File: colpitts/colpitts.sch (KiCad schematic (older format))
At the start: 24 parts

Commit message: Update diseño esquemático
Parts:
- added C? (x2): 100nF, symbol Device:C
- added Q?: 2N3904, Package_TO_SOT_THT:TO-92_Inline, symbol Transistor_BJT:2N3904
- added R? (x4): R, symbol Device:R
- added RV?: R_POT, symbol Device:R_POT
- added U?: LM741, symbol Amplifier_Operational:LM741
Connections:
- net GND: now also C?.1, R?.1, R?.1
- net at JP?.2 (B): now also Q?.2 (B), R?.2
- new net: C?.2, Q?.1 (E), R?.1, R?.2
- new net: C?.2, R?.2, U?.2 (-)
- new net: C?.1, R?.2
- new net +12V: Q?.3 (C)
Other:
- moved on the sheet: C?, J?, JP?, L?, Q?, R?

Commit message: Update diseño esquemático (previa anotación componentes)
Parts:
- removed C?: 100nF, symbol Device:C
- removed R?: R, symbol Device:R
- added C?: 100nF, symbol Device:C
- added C?: 10nF, symbol Device:C
- added J?: BORNERA, symbol Connector_Generic:Conn_01x04
- added R? (x3): 1K, symbol Device:R
- C?: value 100nF -> 100pF
- C?: value 100nF -> 15pF
- C?: value 100nF -> 68pF
- C?: value CTRIM -> TRIM VERDE (5.2pF-30pF)
- C?: value 100nF -> 10pF
- C?: value 100nF -> 33pF
- J?: value Conn_Coaxial -> BNC
- L?: value L -> 40n
- R? (x3): value R -> 10K
- R? (x2): value R -> 330
- R?: value R -> 3.9K
- R?: value R -> 5.6K
- R?: value R -> 1K
- RV?: value R_POT -> 10K
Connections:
- net +12V is gone; now on net +15V: Q?.3 (C)
- net +15V: now also U?.7 (V+), C?.1, J?.4 (Pin_4), R?.2
- net -15V: now also U?.4 (V-), J?.1 (Pin_1)
- net GND: now also C?.1, C?.2, J?.2 (Pin_2), J?.3 (Pin_3), R?.1
- net Vcontrol: now also R?.1, U?.6
- net at Q?.1 (E), R?.2: now also C?.2, R?.1
- net at C?.2, U?.2 (-): now also R?.2
- net at U?.3 (+): now also RV?.2
- net at RV?.1: now also R?.1
- net at RV?.3: now also R?.2
- no-connect marks 0 -> 2
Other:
- moved on the sheet: C?, J?, JP?, L?, Q?, R?, RV?, U?

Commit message: Update diseño esquemático (anotación de componentes)
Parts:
- gave numbers to parts that had none: 37

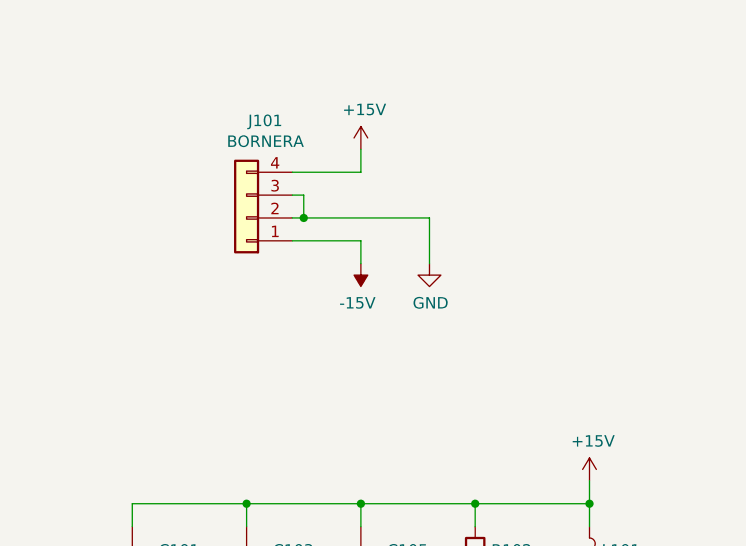
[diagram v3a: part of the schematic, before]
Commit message: ERC - Corrección de errores
1. POWER FLAGS de alimentación.
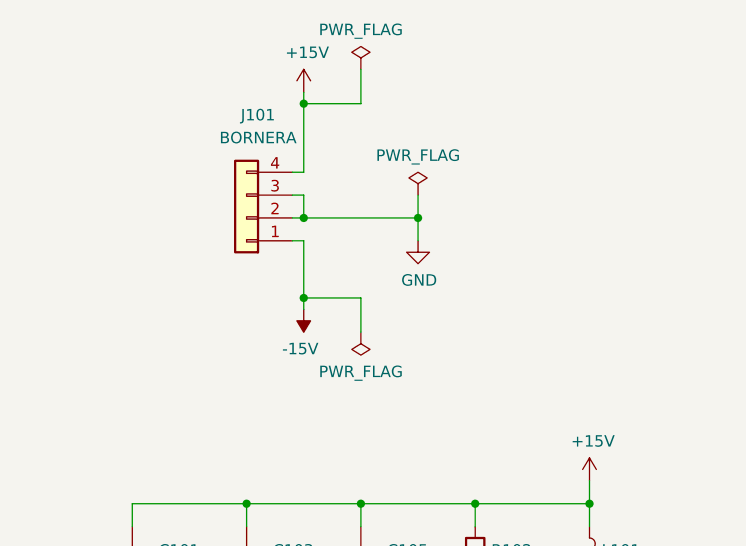
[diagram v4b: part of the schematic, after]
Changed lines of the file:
@@
 Wire Wire Line
 	4500 4250 4500 4300
-$Comp
-L power:GND #PWR0108
-U 1 1 5CF23D89
-P 5000 4800
-F 0 "#PWR0108" H 5000 4550 50  0001 C CNN
-F 1 "GND" H 5005 4627 50  0000 C CNN
-F 2 "" H 5000 4800 50  0001 C CNN
-F 3 "" H 5000 4800 50  0001 C CNN
-	1    5000 4800
-	1    0    0    -1
-$EndComp
 Wire Wire Line
 	5000 4100 5000 4700
@@
 	4500 4700 5000 4700
 Connection ~ 5000 4700
-Wire Wire Line
-	5000 4700 5000 4800
 Wire Wire Line
 	5500 4600 5500 4700
@@
 Wire Wire Line
 	8900 3600 9400 3600
+Wire Wire Line
+	9600 2750 9600 2925
+Wire Wire Line
+	8900 3075 8900 3600
+Wire Wire Line
+	9450 2925 9600 2925
+Connection ~ 9600 2925
+Wire Wire Line
+	9600 2925 9600 3400
+Wire Wire Line
+	9600 2925 10100 2925
+Wire Wire Line
+	10100 2925 10100 3000
+$Comp
+L Device:C C113
+U 1 1 5CFC3836
+P 8000 4100
+F 0 "C113" H 7825 4050 50  0000 C CNN
+F 1 "10nF" H 7800 4150 50  0000 C CNN
+F 2 "" H 8038 3950 50  0001 C CNN
+F 3 "~" H 8000 4100 50  0001 C CNN
+	1    8000 4100
+	-1   0    0    1
+$EndComp
+Connection ~ 8900 3800
+Wire Wire Line
+	8900 3800 9400 3800
+Wire Wire Line
+	8900 4650 8900 4700
+Wire Wire Line
+	8900 4700 10100 4700
+Wire Wire Line
+	10100 3700 10100 4700
+$Comp
+L Connector_Generic:Conn_01x04 J101
+U 1 1 5CFCE8BF
+P 2500 1600
+F 0 "J101" H 2450 1150 50  0000 C CNN
+F 1 "BORNERA" H 2450 1250 50  0000 C CNN
+F 2 "" H 2500 1600 50  0001 C CNN
+F 3 "~" H 2500 1600 50  0001 C CNN
+	1    2500 1600
+	-1   0    0    1
+$EndComp
+$Comp
+L power:+15V #PWR0103
+U 1 1 5CFCFA1F
+P 2750 1050
+F 0 "#PWR0103" H 2750 900 50  0001 C CNN
+F 1 "+15V" H 2765 1223 50  0000 C CNN
+F 2 "" H 2750 1050 50  0001 C CNN
+F 3 "" H 2750 1050 50  0001 C CNN
+	1    2750 1050
+	1    0    0    -1
+$EndComp
+$Comp
+L power:-15V #PWR0104
+U 1 1 5CFCFE1A
+P 2750 2000
+F 0 "#PWR0104" H 2750 2100 50  0001 C CNN
+F 1 "-15V" H 2765 2173 50  0000 C CNN
+F 2 "" H 2750 2000 50  0001 C CNN
+F 3 "" H 2750 2000 50  0001 C CNN
+	1    2750 2000
+	-1   0    0    1
+$EndComp
+Wire Wire Line
+	2700 1600 2750 1600
+Wire Wire Line
+	2700 1500 2750 1500
+Wire Wire Line
+	2750 1500 2750 1600
+Wire Wire Line
+	5000 4700 5000 4800
+$Comp
+L power:GND #PWR0108
+U 1 1 5CF23D89
+P 5000 4800
+F 0 "#PWR0108" H 5000 4550 50  0001 C CNN
+F 1 "GND" H 5005 4627 50  0000 C CNN
+F 2 "" H 5000 4800 50  0001 C CNN
+F 3 "" H 5000 4800 50  0001 C CNN
+	1    5000 4800
+	1    0    0    -1
+$EndComp
 $Comp
 L power:GND #PWR0115
@@
 	1    0    0    -1
 $EndComp
-Wire Wire Line
-	9600 2750 9600 2925
-Wire Wire Line
-	8900 3075 8900 3600
-Wire Wire Line
-	9450 2925 9600 2925
-Connection ~ 9600 2925
-Wire Wire Line
-	9600 2925 9600 3400
-Wire Wire Line
-	9600 2925 10100 2925
-Wire Wire Line
-	10100 2925 10100 3000
-$Comp
-L Device:C C113
-U 1 1 5CFC3836
-P 8000 4100
-F 0 "C113" H 7825 4050 50  0000 C CNN
-F 1 "10nF" H 7800 4150 50  0000 C CNN
-F 2 "" H 8038 3950 50  0001 C CNN
-F 3 "~" H 8000 4100 50  0001 C CNN
-	1    8000 4100
-	-1   0    0    1
-$EndComp
-Connection ~ 8900 3800
-Wire Wire Line
-	8900 3800 9400 3800
-Wire Wire Line
-	8900 4650 8900 4700
-Wire Wire Line
-	8900 4700 10100 4700
-Wire Wire Line
-	10100 3700 10100 4700
-$Comp
-L Connector_Generic:Conn_01x04 J101
-U 1 1 5CFCE8BF
-P 2500 1600
-F 0 "J101" H 2418 1175 50  0000 C CNN
-F 1 "BORNERA" H 2418 1266 50  0000 C CNN
-F 2 "" H 2500 1600 50  0001 C CNN
-F 3 "~" H 2500 1600 50  0001 C CNN
-	1    2500 1600
-	-1   0    0    1
-$EndComp
-$Comp
-L power:+15V #PWR0103
-U 1 1 5CFCFA1F
-P 3000 1300
-F 0 "#PWR0103" H 3000 1150 50  0001 C CNN
-F 1 "+15V" H 3015 1473 50  0000 C CNN
-F 2 "" H 3000 1300 50  0001 C CNN
-F 3 "" H 3000 1300 50  0001 C CNN
-	1    3000 1300
-	1    0    0    -1
-$EndComp
-$Comp
-L power:-15V #PWR0104
-U 1 1 5CFCFE1A
-P 3000 1800
-F 0 "#PWR0104" H 3000 1900 50  0001 C CNN
-F 1 "-15V" H 3015 1973 50  0000 C CNN
-F 2 "" H 3000 1800 50  0001 C CNN
-F 3 "" H 3000 1800 50  0001 C CNN
-	1    3000 1800
-	-1   0    0    1
-$EndComp
 $Comp
 L power:GND #PWR0105
 U 1 1 5CFD0749
-P 3300 1800
-F 0 "#PWR0105" H 3300 1550 50  0001 C CNN
-F 1 "GND" H 3305 1627 50  0000 C CNN
-F 2 "" H 3300 1800 50  0001 C CNN
-F 3 "" H 3300 1800 50  0001 C CNN
-	1    3300 1800
-	1    0    0    -1
-$EndComp
-Wire Wire Line
-	2700 1400 3000 1400
-Wire Wire Line
-	3000 1400 3000 1300
-Wire Wire Line
-	2700 1600 2750 1600
-Wire Wire Line
-	3300 1600 3300 1800
-Wire Wire Line
-	2700 1500 2750 1500
-Wire Wire Line
-	2750 1500 2750 1600
+P 3250 1700
+F 0 "#PWR0105" H 3250 1450 50  0001 C CNN
+F 1 "GND" H 3255 1527 50  0000 C CNN
+F 2 "" H 3250 1700 50  0001 C CNN
+F 3 "" H 3250 1700 50  0001 C CNN
+	1    3250 1700
+	1    0    0    -1
+$EndComp
+$Comp
+L power:PWR_FLAG #FLG0101
+U 1 1 5D007D00
+P 3000 2100
+F 0 "#FLG0101" H 3000 2175 50  0001 C CNN
+F 1 "PWR_FLAG" H 3000 2273 50  0000 C CNN
+F 2 "" H 3000 2100 50  0001 C CNN
+F 3 "~" H 3000 2100 50  0001 C CNN
+	1    3000 2100
+	-1   0    0    1
+$EndComp
+$Comp
+L power:PWR_FLAG #FLG0102
+U 1 1 5D008F68
+P 3250 1500
+F 0 "#FLG0102" H 3250 1575 50  0001 C CNN
+F 1 "PWR_FLAG" H 3250 1673 50  0000 C CNN
+F 2 "" H 3250 1500 50  0001 C CNN
+F 3 "~" H 3250 1500 50  0001 C CNN
+	1    3250 1500
+	1    0    0    -1
+$EndComp
+Wire Wire Line
+	2700 1400 2750 1400
+Wire Wire Line
+	2750 1400 2750 1100
+$Comp
+L power:PWR_FLAG #FLG0103
+U 1 1 5D007236
+P 3000 950
+F 0 "#FLG0103" H 3000 1025 50  0001 C CNN
+F 1 "PWR_FLAG" H 3000 1123 50  0000 C CNN
+F 2 "" H 3000 950 50  0001 C CNN
+F 3 "~" H 3000 950 50  0001 C CNN
+	1    3000 950
+	1    0    0    -1
+$EndComp
+Wire Wire Line
+	3000 950  3000 1100
+Wire Wire Line
+	3000 1100 2750 1100
+Connection ~ 2750 1100
+Wire Wire Line
+	2750 1100 2750 1050
+Wire Wire Line
+	2700 1700 2750 1700
+Wire Wire Line
+	2750 1700 2750 1950
+Wire Wire Line
+	3000 2100 3000 1950
+Wire Wire Line
+	3000 1950 2750 1950
+Connection ~ 2750 1950
+Wire Wire Line
+	2750 1950 2750 2000
+Wire Wire Line
+	3250 1700 3250 1600
+Wire Wire Line
+	3250 1600 2750 1600
 Connection ~ 2750 1600
 Wire Wire Line
-	2750 1600 3300 1600
-Wire Wire Line
-	2700 1700 3000 1700
-Wire Wire Line
-	3000 1700 3000 1800
+	3250 1600 3250 1500
+Connection ~ 3250 1600
 $EndSCHEMATC

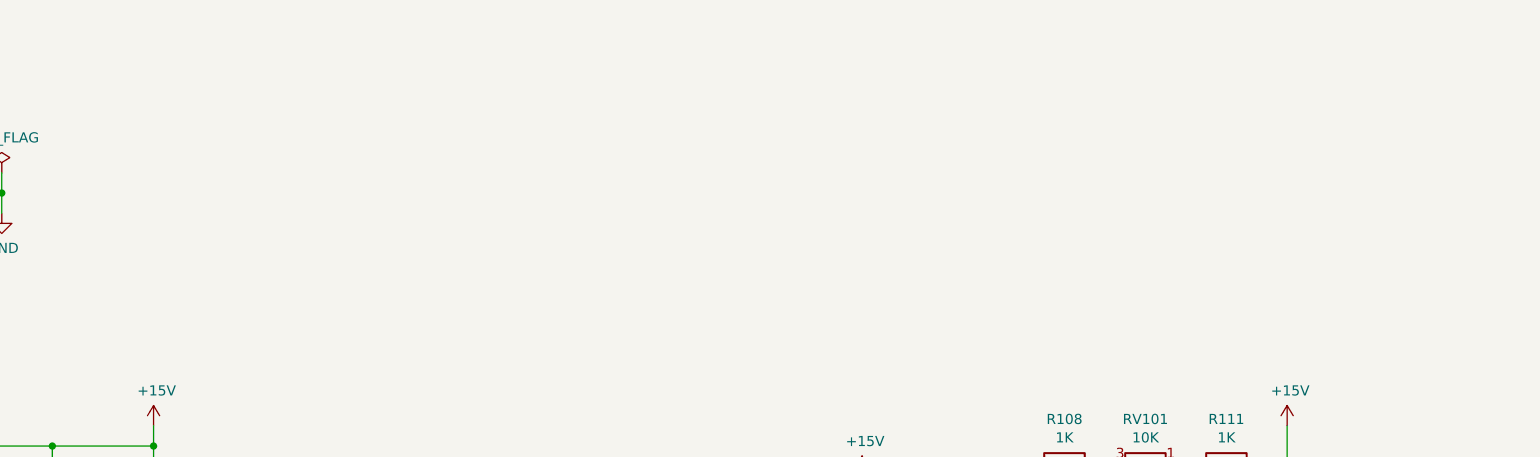
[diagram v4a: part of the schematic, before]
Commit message: Update diseño esquemático (previa asignación de huellas)
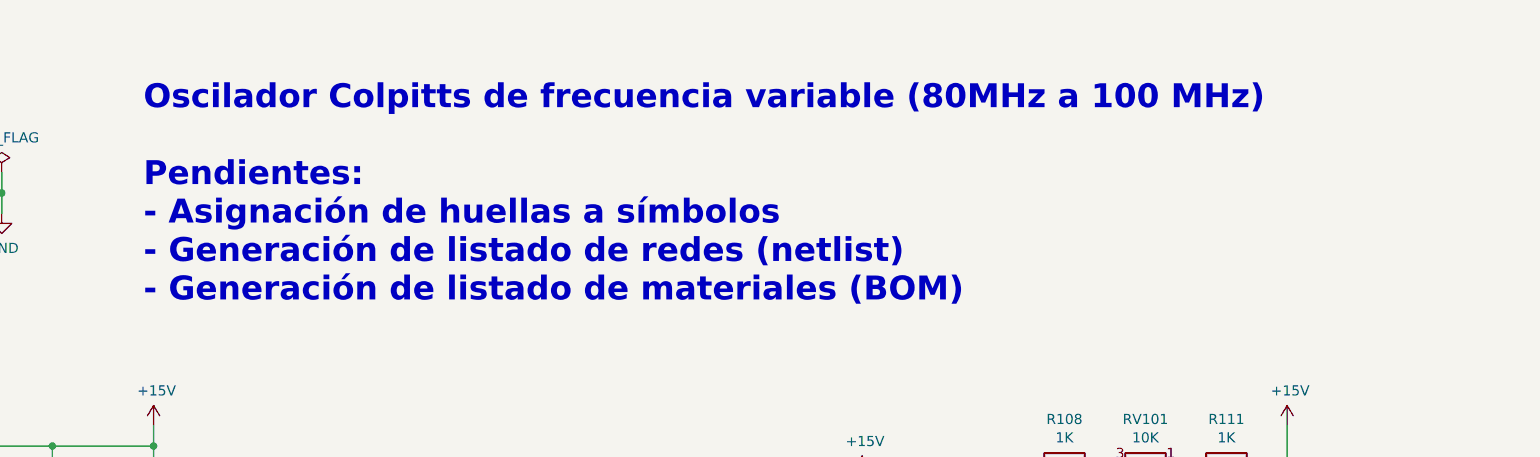
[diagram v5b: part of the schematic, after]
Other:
- note added: "Oscilador Colpitts de frecuencia variable (80MHz a 100 MHz)\n\nPendientes:\n- Asignación de huellas a símbolos\n- Generación de listado de redes (netlist)\n- Generación de listado de materiales (BOM)"
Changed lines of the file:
@@
 Text Label 6050 4250 2    79   Italic 16
 Vout
-Text Label 1500 4950 0    50   ~ 0
-Vcontrol
 $Comp
 L power:GND #PWR0109
@@
 	3250 1600 3250 1500
 Connection ~ 3250 1600
+Text Notes 3950 2150 0    118  ~ 24
+Oscilador Colpitts de frecuencia variable (80MHz a 100 MHz)\n\nPendientes:\n- Asignación de huellas a símbolos\n- Generación de listado de redes (netlist)\n- Generación de listado de materiales (BOM)
+Text Label 1500 4950 0    50   ~ 0
+Vcontrol
 $EndSCHEMATC
